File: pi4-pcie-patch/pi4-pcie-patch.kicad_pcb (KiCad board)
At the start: 2 copper layers, 7.6 x 7.6 mm, 12 parts

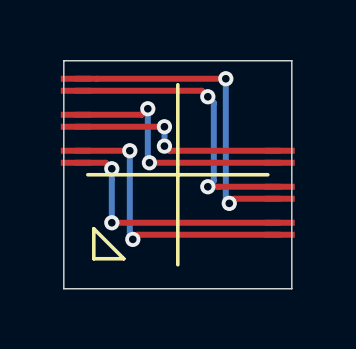
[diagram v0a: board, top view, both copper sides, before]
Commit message: pi4-pcie-patch: add castellations
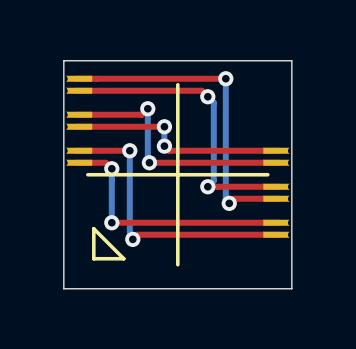
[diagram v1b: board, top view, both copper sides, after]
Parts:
- TP21, TP22, TP24, TP25, TP27, TP28, TP52, TP53, TP55, TP56, TP58, TP59: footprint pi4-pcie-patch:PAD_0.2_1.0MM -> pi4-pcie-patch:PAD_0.2_1.0MM_CAST
- moved TP21 0.40 mm to (87.8, 66.0), turned to 180 degrees
- moved TP22 0.40 mm to (87.8, 65.6), turned to 180 degrees
- moved TP24 0.40 mm to (87.8, 64.8), turned to 180 degrees
- moved TP25 0.40 mm to (87.8, 64.4), turned to 180 degrees
- moved TP27 0.40 mm to (87.8, 63.6), turned to 180 degrees
- moved TP28 0.40 mm to (87.8, 63.2), turned to 180 degrees
- moved TP52 0.40 mm to (80.2, 60.8)
- moved TP53 0.40 mm to (80.2, 61.2)
- moved TP55 0.40 mm to (80.2, 62.0)
- moved TP56 0.40 mm to (80.2, 62.4)
- moved TP58 0.40 mm to (80.2, 63.2)
- moved TP59 0.40 mm to (80.2, 63.6)
